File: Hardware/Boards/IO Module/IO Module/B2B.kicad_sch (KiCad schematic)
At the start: 2 parts, among them J2 LSHM-130-XX.X-XXX-DV-A-S-K-XX, J3 LSHM-130-XX.X-XXX-DV-A-S-K-XX

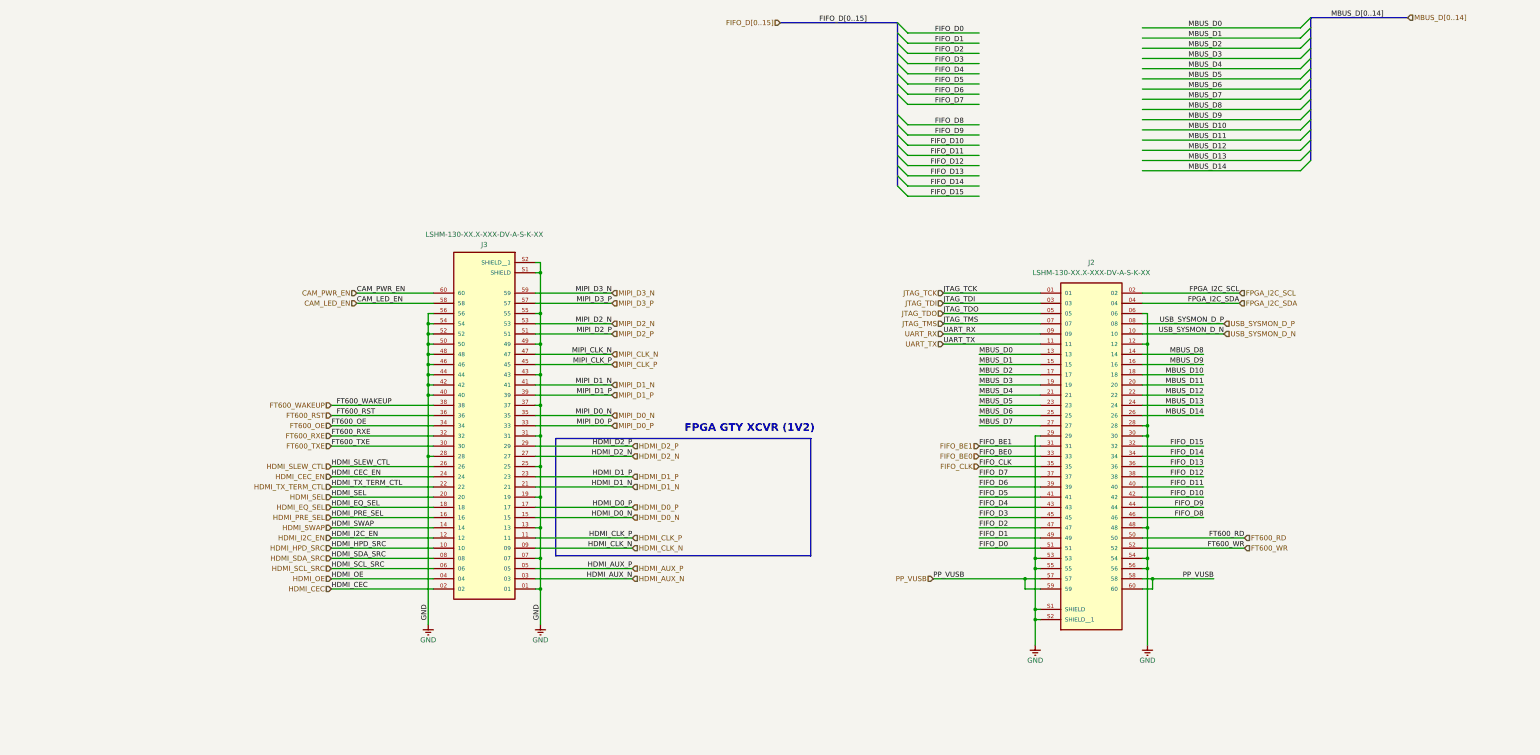
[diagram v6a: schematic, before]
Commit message: Added pin voltages to IO module b2b
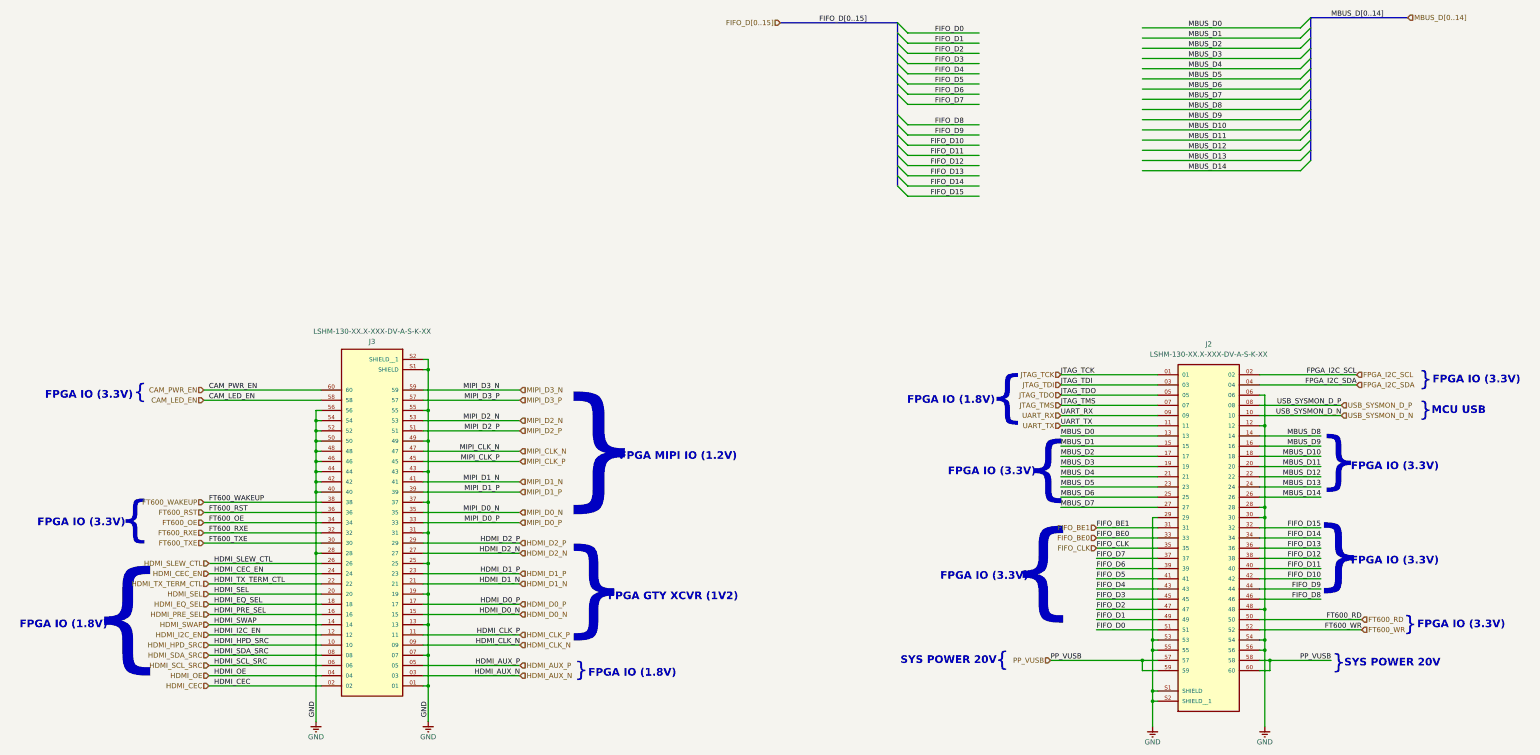
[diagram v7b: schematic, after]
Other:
- note added: "FPGA IO (1.8V)"
- note added: "FPGA IO (3.3V)"
- note added: "FPGA MIPI IO (1.2V)"
- note added: "MCU USB"
- note added: "SYS POWER 20V"
- note added: "{"
- note added: "}"
- moved on the sheet: J2, J3

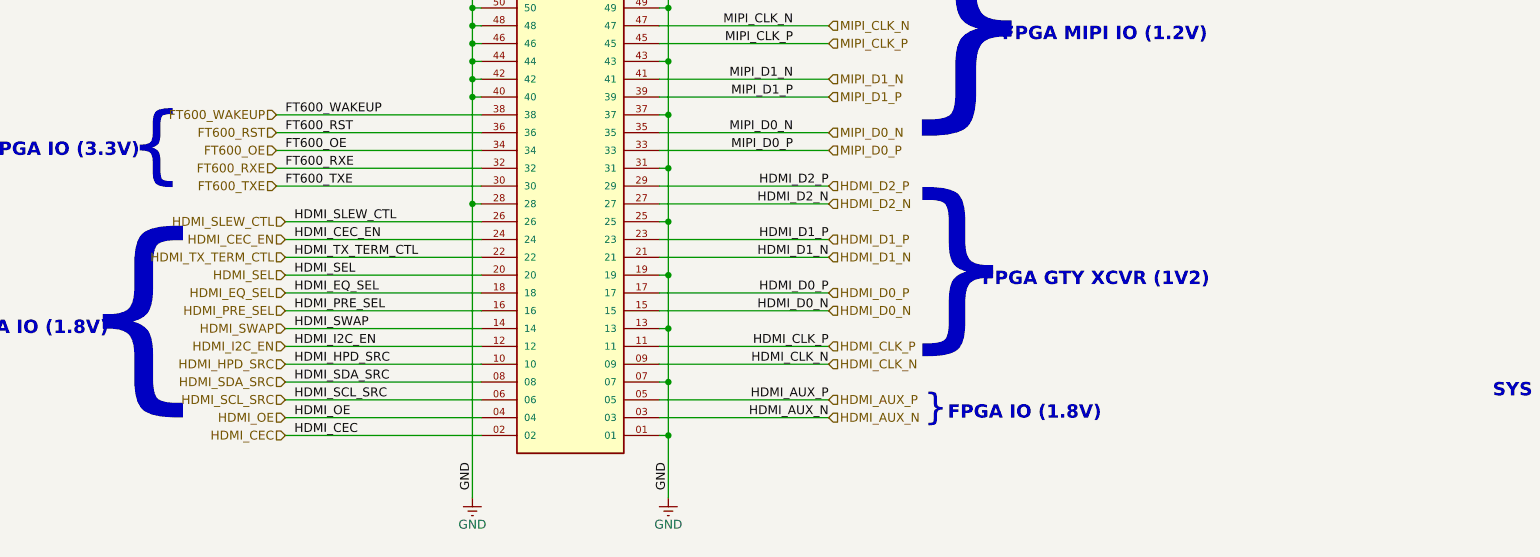
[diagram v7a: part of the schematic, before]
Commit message: Using new DP to HDMI IC
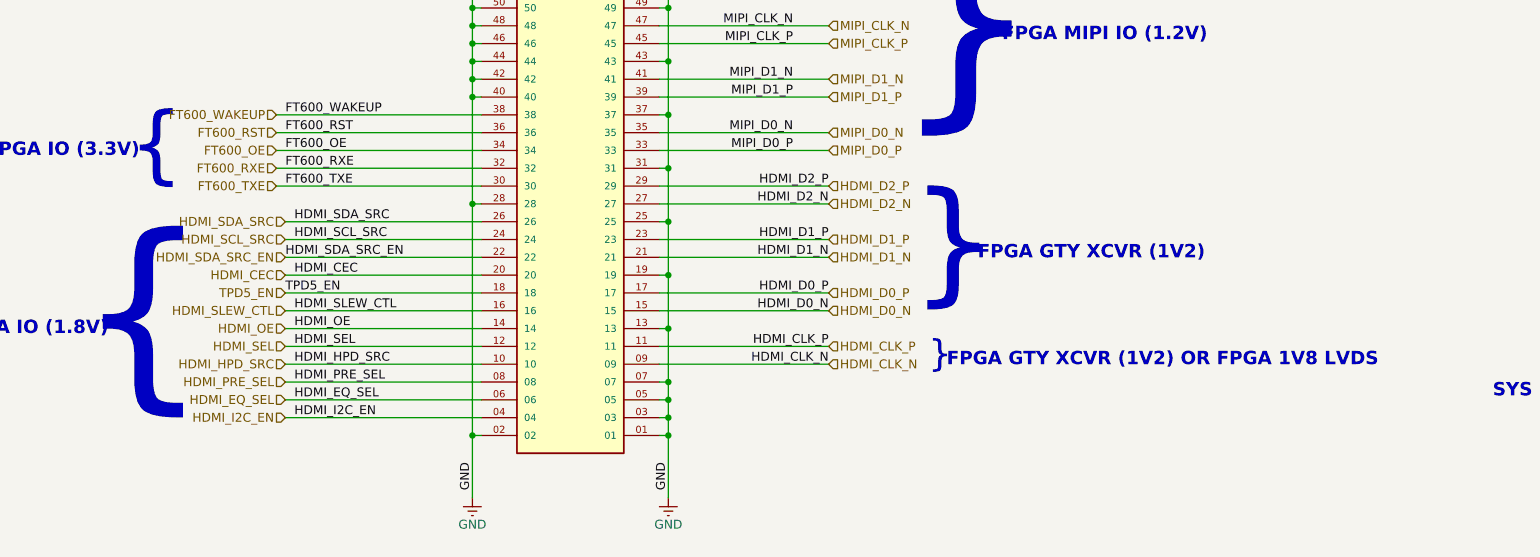
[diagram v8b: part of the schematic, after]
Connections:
- net HDMI_AUX_N is gone; now on net GND: J3.03
- net HDMI_AUX_P is gone; now on net GND: J3.05
- net HDMI_CEC_EN is gone; now on net HDMI_SCL_SRC: J3.24
- net HDMI_SWAP is gone; now on net HDMI_OE: J3.14
- net GND: now also J3.02
- net HDMI_CEC: now also J3.20; no longer J3.02
- net HDMI_EQ_SEL: now also J3.06; no longer J3.18
- net HDMI_I2C_EN: now also J3.04; no longer J3.12
- net HDMI_OE: no longer J3.04
- net HDMI_PRE_SEL: now also J3.08; no longer J3.16
- net HDMI_SCL_SRC: no longer J3.06
- net HDMI_SDA_SRC: now also J3.26; no longer J3.08
- net HDMI_SEL: now also J3.12; no longer J3.20
- net HDMI_SLEW_CTL: now also J3.16; no longer J3.26
- net HDMI_TX_TERM_CTL renamed HDMI_SDA_SRC_EN
- new net TPD5_EN: J3.18
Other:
- note added: "FPGA GTY XCVR (1V2) OR FPGA 1V8 LVDS"
